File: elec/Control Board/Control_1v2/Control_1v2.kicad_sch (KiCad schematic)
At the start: 168 parts, among them J1 DB9_Female_MountingHoles, J10 Conn_02x12_Odd_Even, J11 Con_01x02_2.5mm, J14 Conn_01x10, J2 Conn_01x08, J25 Con_01x02_2.5mm, J26 Conn_01x10, J27 Conn_02x12_Odd_Even, J28 Con_01x02_2.5mm, J29 Conn_01x10, J3 Conn_01x08, J37 Conn_01x04, J4 Conn_01x08, J5 Conn_01x08, J6 Conn_01x08, J7 Conn_01x10, J8 Conn_02x18_Odd_Even, J9 Conn_01x10, Q601 BSS138

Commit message: PCB V1.2. Add 3d model for power supply footprint. Set many headers connectors for DNI on schematic and PCB.
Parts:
- J1, J2, J27, J3, J4, J5, J6, J7, J8: now not fitted; now left out of the parts list
- J9: now left out of the parts list
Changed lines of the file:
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@@
   )
   (symbol (lib_id "Connector_Generic:Conn_02x18_Odd_Even") (at 351.79 142.24 0) (mirror y) (unit 1)
-    (in_bom yes) (on_board yes) (dnp no)
+    (in_bom no) (on_board yes) (dnp yes)
     (property "Reference" "J8" (at 350.52 115.57 0)
       (effects (font (size 1.27 1.27)))
@@
   )
   (symbol (lib_id "Connector_Generic:Conn_01x10") (at 419.1 50.8 0) (mirror y) (unit 1)
-    (in_bom yes) (on_board yes) (dnp yes)
+    (in_bom no) (on_board yes) (dnp yes)
     (property "Reference" "J9" (at 419.1 36.83 0)
       (effects (font (size 1.27 1.27)))
@@
   )
   (symbol (lib_id "Connector_Generic:Conn_01x08") (at 171.45 165.1 0) (mirror y) (unit 1)
-    (in_bom yes) (on_board yes) (dnp no)
+    (in_bom no) (on_board yes) (dnp yes)
     (property "Reference" "J3" (at 167.64 165.1 0)
       (effects (font (size 1.27 1.27)))
@@
   )
   (symbol (lib_id "Connector_Generic:Conn_01x08") (at 184.15 137.16 0) (mirror y) (unit 1)
-    (in_bom yes) (on_board yes) (dnp no) (fields_autoplaced)
+    (in_bom no) (on_board yes) (dnp yes) (fields_autoplaced)
     (property "Reference" "J4" (at 184.15 123.19 0)
       (effects (font (size 1.27 1.27)))
@@
   )
   (symbol (lib_id "Connector_Generic:Conn_01x08") (at 160.02 76.2 180) (unit 1)
-    (in_bom yes) (on_board yes) (dnp no) (fields_autoplaced)
+    (in_bom no) (on_board yes) (dnp yes) (fields_autoplaced)
     (property "Reference" "J2" (at 160.02 59.69 0)
       (effects (font (size 1.27 1.27)))
@@
   )
   (symbol (lib_id "Connector_Generic:Conn_01x08") (at 194.31 116.84 0) (mirror y) (unit 1)
-    (in_bom yes) (on_board yes) (dnp no)
+    (in_bom no) (on_board yes) (dnp yes)
     (property "Reference" "J5" (at 190.5 108.585 0)
       (effects (font (size 1.27 1.27)))
@@
   )
   (symbol (lib_id "Connector:DB9_Female_MountingHoles") (at 64.77 60.96 180) (unit 1)
-    (in_bom yes) (on_board yes) (dnp no) (fields_autoplaced)
+    (in_bom no) (on_board yes) (dnp yes) (fields_autoplaced)
     (property "Reference" "J1" (at 59.69 59.6899 0)
       (effects (font (size 1.27 1.27)) (justify left))
@@
   )
   (symbol (lib_id "Connector_Generic:Conn_02x12_Odd_Even") (at 450.85 124.46 0) (mirror y) (unit 1)
-    (in_bom yes) (on_board yes) (dnp no)
+    (in_bom no) (on_board yes) (dnp yes)
     (property "Reference" "J27" (at 449.58 106.68 0)
       (effects (font (size 1.27 1.27)))
@@
   )
   (symbol (lib_id "Connector_Generic:Conn_01x10") (at 345.44 91.44 0) (unit 1)
-    (in_bom yes) (on_board yes) (dnp no)
+    (in_bom no) (on_board yes) (dnp yes)
     (property "Reference" "J7" (at 345.44 78.74 0)
       (effects (font (size 1.27 1.27)))
@@
   )
   (symbol (lib_id "Connector_Generic:Conn_01x08") (at 308.61 68.58 0) (unit 1)
-    (in_bom yes) (on_board yes) (dnp no)
+    (in_bom no) (on_board yes) (dnp yes)
     (property "Reference" "J6" (at 304.8 55.372 0)
       (effects (font (size 1.27 1.27)) (justify left))

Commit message: Add a 3D model for the JHT connector B2B-XH-A-GU.
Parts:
- J11, J25, J28: footprint Connector_JST:JST_XH_B2B-XH-AM_1x02_P2.50mm_Vertical -> PubInv_KiCad_PCB:JST_XH_B2B-XH-AM_1x02_P2.50mm_Vertical
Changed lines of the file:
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@@
       (effects (font (size 1.27 1.27)) (justify left))
     )
-    (property "Footprint" "Connector_JST:JST_XH_B2B-XH-AM_1x02_P2.50mm_Vertical" (at 482.6 207.01 0)
+    (property "Footprint" "PubInv_KiCad_PCB:JST_XH_B2B-XH-AM_1x02_P2.50mm_Vertical" (at 482.6 207.01 0)
       (effects (font (size 1.27 1.27)) hide)
     )
@@
       (effects (font (size 1.27 1.27)) (justify left))
     )
-    (property "Footprint" "Connector_JST:JST_XH_B2B-XH-AM_1x02_P2.50mm_Vertical" (at 482.6 172.72 0)
+    (property "Footprint" "PubInv_KiCad_PCB:JST_XH_B2B-XH-AM_1x02_P2.50mm_Vertical" (at 482.6 172.72 0)
       (effects (font (size 1.27 1.27)) hide)
     )
@@
       (effects (font (size 1.27 1.27)) (justify left))
     )
-    (property "Footprint" "Connector_JST:JST_XH_B2B-XH-AM_1x02_P2.50mm_Vertical" (at 482.6 21.59 0)
+    (property "Footprint" "PubInv_KiCad_PCB:JST_XH_B2B-XH-AM_1x02_P2.50mm_Vertical" (at 482.6 21.59 0)
       (effects (font (size 1.27 1.27)) hide)
     )
@@
       (effects (font (size 1.27 1.27)) (justify left))
     )
-    (property "Footprint" "Connector_JST:JST_XH_B2B-XH-AM_1x02_P2.50mm_Vertical" (at 482.6 92.71 0)
+    (property "Footprint" "PubInv_KiCad_PCB:JST_XH_B2B-XH-AM_1x02_P2.50mm_Vertical" (at 482.6 92.71 0)
       (effects (font (size 1.27 1.27)) hide)
     )

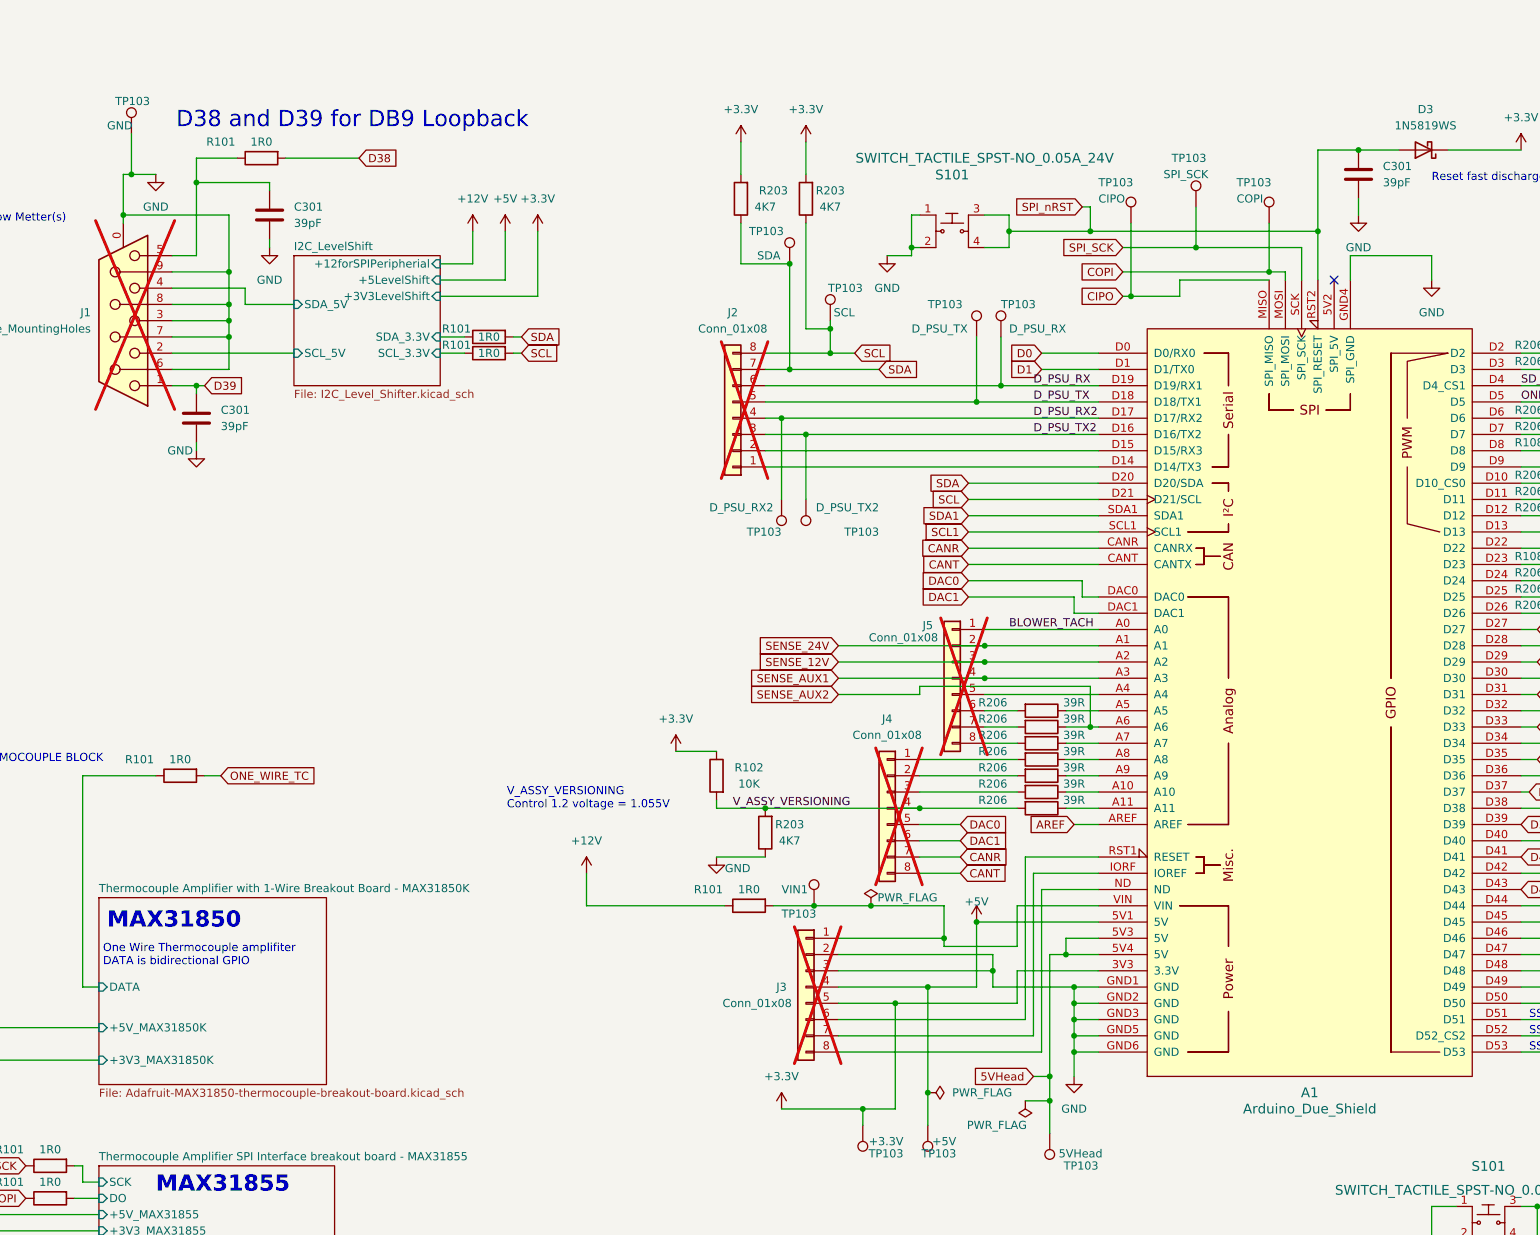
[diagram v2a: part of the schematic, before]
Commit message: PCB V1.2. Add test points of many colors.
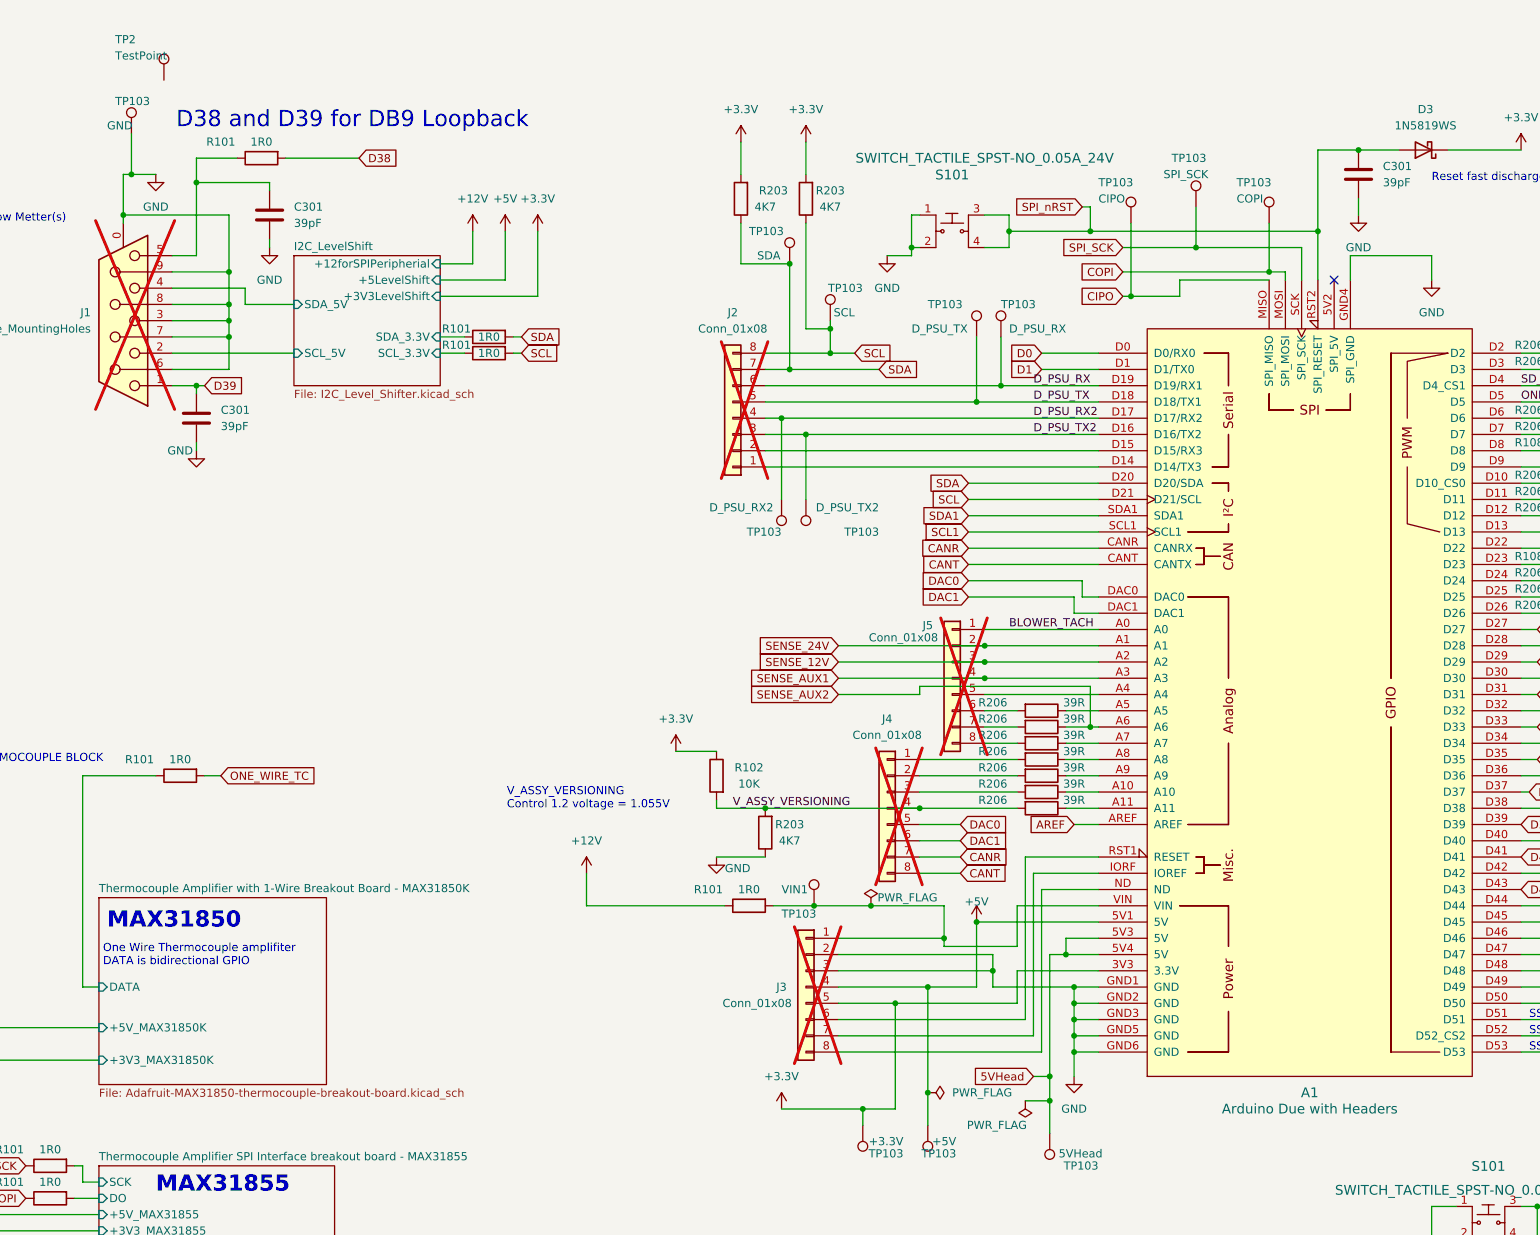
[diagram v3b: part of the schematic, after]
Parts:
- added TP2: TestPoint, TestPoint:TestPoint_Loop_D2.54mm_Drill1.5mm_Beaded, symbol Connector:TestPoint
- A1: value Arduino_Due_Shield -> Arduino Due with Headers; Cost (none) -> 48.40; Distributor 1 (none) -> AMAZON.COM; Distributor 1 PN (none) -> https://www.amazon.com/Arduino-org-A000062-Arduino-Due/dp/B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; MPN (none) -> DUE; Manufacturer (none) -> Arduino
- TP103: Cost NA -> 0.0714; Distributor 1 (none) -> JLCPCB; Distributor 1 PN (none) -> C5199804; MPN (none) -> RH-5004; Manufacturer (none) -> ronghe
- TP103: Cost NA -> 0.1865; Distributor 1 (none) -> JLCPCB; Distributor 1 PN (none) -> C7589090; MPN (none) -> RH-5121; Manufacturer (none) -> ronghe
- TP103: Cost NA -> 0.0696; Distributor 1 (none) -> JLCPCB; Distributor 1 PN (none) -> C5277086; MPN (none) -> RH-5000; Manufacturer (none) -> ronghe
- TP103: Cost 0 -> 0.0792; Distributor 1 (none) -> JLCPCB; Distributor 1 PN (none) -> C5199807; MPN (none) -> RH-5117; Manufacturer (none) -> ronghe
- TP103: Cost 0 -> 0.0696; Distributor 1 (none) -> JLCPCB; Distributor 1 PN (none) -> C5277086; MPN (none) -> RH-5000; Manufacturer (none) -> ronghe
- TP103: Cost 0 -> 0.1865; Distributor 1 (none) -> JLCPCB; Distributor 1 PN (none) -> C5199812; MPN (none) -> RH-5007; Manufacturer (none) -> ronghe
- TP103: Cost 0 -> 0.0714; Distributor 1 (none) -> JLCPCB; Distributor 1 PN (none) -> C5199804; MPN (none) -> RH-5004; Manufacturer (none) -> ronghe

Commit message: PCB V1.2. Work up first BOM / PL file.
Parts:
- added *_Comment: Comment, Footprint, symbol GPAD_SCH_LIB:PCB_GPAD_VER1
- MF3: Distributor 1 Amazon -> AMAZON.COM
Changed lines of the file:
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@@
     )
   )
+  (symbol (lib_id "GPAD_SCH_LIB:PCB_GPAD_VER1") (at 294.64 259.08 0) (unit 1)
+    (in_bom yes) (on_board no) (dnp no)
+    (property "Reference" "*_Comment" (at 292.1 247.65 0)
+      (effects (font (size 1.27 1.27)) (justify left))
+    )
+    (property "Value" "Comment" (at 278.13 276.86 0)
+      (effects (font (size 1.27 1.27)) (justify left))
+    )
+    (property "Footprint" "Footprint " (at 294.64 259.08 0)
+      (effects (font (size 1.27 1.27)) hide)
+    )
+    (property "Datasheet" "" (at 294.64 259.08 0)
+      (effects (font (size 0 0)) hide)
+    )
+    (property "Distributor 1" "JLCPCB" (at 294.64 259.08 0)
+      (effects (font (size 1.27 1.27)) hide)
+    )
+    (property "Distributor 1 PN" "JLCPCB Part # " (at 294.64 259.08 0)
+      (effects (font (size 0 0)) hide)
+    )
+    (property "Cost" "0" (at 294.64 259.08 0)
+      (effects (font (size 1.27 1.27)) hide)
+    )
+    (property "Description" "Headers for JLCPCB BOM / PL" (at 294.64 259.08 0)
+      (effects (font (size 1.27 1.27)) hide)
+    )
+    (property "MPN" "na" (at 294.64 259.08 0)
+      (effects (font (size 1.27 1.27)) hide)
+    )
+    (property "LongLead" "na" (at 294.64 259.08 0)
+      (effects (font (size 1.27 1.27)) hide)
+    )
+    (property "Manufacturer" "PublicInvention" (at 294.64 259.08 0)
+      (effects (font (size 1.27 1.27)) hide)
+    )
+    (instances
+      (project "Control_1v2"
+        (path "/c68c9deb-8d4d-42f0-adf8-4d3022f4ee59"
+          (reference "*_Comment") (unit 1)
+        )
+      )
+    )
+  )
   (symbol (lib_id "Device:R") (at 509.27 134.62 0) (mirror y) (unit 1)
     (in_bom yes) (on_board yes) (dnp no)
@@
       (effects (font (size 0 0)) hide)
     )
-    (property "Distributor 1" "Amazon" (at 246.38 289.56 0)
+    (property "Distributor 1" "AMAZON.COM" (at 246.38 289.56 0)
       (effects (font (size 1.27 1.27)) hide)
     )
